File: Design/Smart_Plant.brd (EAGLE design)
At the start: 80 x 111.8 mm, 85 parts, among them IC1 NE555D, Q1 IRLML0100, Q3 2.5A/30V, Q4 MBT3904DW1T1, U10 ESP3212, U6 W25Q32FVSS, U7 FT231XS, U8 MCP73831, U9 AP2112K-3.3V, X2 MICROSD, Y3 26MHz

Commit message: Updated design files for Smart_Plant
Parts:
- removed C29, C30: 10pF, SparkFun-Capacitors:0603
- removed C31, C32: 270pF, esp32-thing-temp:0603
- removed C33: 10nF, SparkFun-Capacitors:0603
- removed C34, C37, C38, C41, C48, C49, C51, C53: 0.1uF, SparkFun-Capacitors:0603
- removed C35: 2.4pF, esp32-thing-temp:0603
- removed C36: 5.6pF, esp32-thing-temp:0603
- removed C39, C40: 47pF, SparkFun-Capacitors:0603
- removed C42: 4.7uF, SparkFun-Capacitors:0603-CAP
- removed C43: 1.0uF, SparkFun-Capacitors:0805
- removed C44: 2.2uF, SparkFun-Capacitors:0603
- removed C45, C46: 4.7uF, SparkFun-Capacitors:0603
- removed C47: 100pF, SparkFun-Capacitors:0603
- removed C50: 10uF, SparkFun-Capacitors:0603
- removed C52: 1.0uF, SparkFun-Capacitors:0603
- removed C56: 3.0nF, esp32-thing-temp:0603
- removed D10, D9: MBR0530, microbuilder:SOD-123
- removed D5: BAT20J, SparkFun-DiscreteSemi:SOD-323
- removed D6: Yellow, SparkFun-LED:LED-0603
- removed D7: Green, SparkFun-LED:LED-0603
- removed E2: ANTENNA, esp32-thing-temp:TRACE_ANTENNA_2.4GHZ_25.7MM_TUNED
- removed EINK1: EINK_24PIN_290IN, microbuilder:EINK_290IN
- removed F2: 500mA, SparkFun-PowerIC:PTC-1206
- removed JP1: (no value), SparkFun-Connectors:USB-B-MICRO-SMD_V03
- removed JP3: LiPo, SparkFun-Connectors:JST-2-PTH
- removed L2: 2.7nH, SparkFun-Passives:0603
- removed Q3: 2.5A/30V, SparkFun-DiscreteSemi:SOT23-3
- removed Q4: MBT3904DW1T1, esp32-thing-temp:SC70-6
- removed R19, R24: 1K, SparkFun-Resistors:0603
- removed R20: 2.0k, SparkFun-Resistors:0603
- removed R21: DNP, SparkFun-Passives:1/6W-RES
- removed R22, R23, R26: 10k, SparkFun-Resistors:0603
- removed R27: DNP, microbuilder:0805_10MGAP
- removed S3: RESET, SparkFun-Electromechanical:TACTILE_SWITCH_SMD_4.6X2.8MM
- removed S4: BTN-0, SparkFun-Electromechanical:TACTILE_SWITCH_SMD_4.6X2.8MM
- removed SJ4: (no value), SparkFun-Passives:PAD-JUMPER-3-2OF3_NC_BY_TRACE_YES_SILK_FULL_BOX
- removed SJ5: JUMPER-PAD-2-NC_BY_TRACE, SparkFun-Passives:PAD-JUMPER-2-NC_BY_TRACE_YES_SILK
- removed U10: ESP3212, esp32-thing-temp:QFN48-0.4MM
- removed U6: W25Q32FVSS, SparkFun-DigitalIC:SOIC-8
- removed U7: FT231XS, SparkFun-DigitalIC:SSOP20_L
- removed U8: MCP73831, SparkFun-PowerIC:SOT23-5
- removed U9: AP2112K-3.3V, SparkFun-PowerIC:SOT23-5
- removed X2: MICROSD, microbuilder:MICROSD
- removed Y3: 26MHz, things:CRYSTAL-SMD-3.2X2.5
- added BT1: (no value), SparkFun-Batteries:BATTCOM_20MM_PTH
- added C10, C16, C4: 10uF, rcl:C0603
- added C11, C6: 100nF, rcl:C0603
- added C12: 22uF, rcl:C0603
- added C15: 0.1uF, rcl:C0603
- added C5: 10nF, rcl:C0603
- added C7: 1uF, rcl:C0603
- added D1, D2, D3: SS14, SparkFun-DiscreteSemi:SMA-DIODE
- added FPC: E-PAPER-FPC, SpaceDIY_connectors:FPC-05FB-24PH20
- added IC2: TLC555CDR, linear:SO08
- added IC3: AHT20, SamacSys_Parts:AHT20
- added IC4: TP4056, TP4056:SOT23-8
- added J1: (no value), SparkFun-Connectors:1X02
- added J3: (no value), pinhead:1X04
- added LED1: Red, SpaceDIY_semiconductors:LED_0603
- added LED2: Green, SpaceDIY_semiconductors:LED_0603
- added Q2: ALS-PT19-315C, SparkFun-DiscreteSemi:PT17-21C-L41-TR8
- added R14, R7: 10k, rcl:R0603
- added R17: 220, rcl:R0603
- added R4: 33k, rcl:R0603
- added R5: 1K, rcl:R0603
- added R6: 1k, rcl:R0603
- added R8: 1M, rcl:R0603
- added R9: 10K, rcl:R0603
- added S1: Flash, SpaceDIY_electromechanical:TACTILE_SWITCH_SMD_5.2MM
- added S2: Reset, SpaceDIY_electromechanical:TACTILE_SWITCH_SMD_5.2MM
- added T1: MMBT2222A, JLC PCB Basic Parts_loc:SOT23
- added T2: LBSS84LT1G, JLC PCB Basic Parts_loc:SOT23
- added TP1, TP2: TPB1,27, testpad:B1,27
- added U1: ESP-32S, esp32:ESP-32S
- C1: value 0.1uF -> 10uF; device SparkFun-Capacitors:0603 -> rcl:C0603
- C13, C14, C17, C18, C19, C25, C27, C28, C9: device microbuilder:0805-NO -> rcl:C0603
- C2: value 0.1uF -> 4.7uF; device SparkFun-Capacitors:0603 -> rcl:C0603
- C26: value 4.7uF/25V -> 4.7uF; device microbuilder:0805-NO -> rcl:C0603
- C3: value 0.1uF -> 0.47nF; device SparkFun-Capacitors:0603 -> rcl:C0603
- C8: value 10uF/10V+ -> 10uF; device microbuilder:0805-NO -> rcl:C0603
- D4: value MBR0530 -> LL4148; device microbuilder:SOD-123 -> SpaceDIY_semiconductors:LL-34
- IC1: value NE555D -> AMS1117-3.3; device linear:SO08 -> SparkFun-IC-Power:SOT223
- R1, R12, R15: value 27 -> 10k; device SparkFun-Resistors:0603 -> rcl:R0603
- R10, R16: device SparkFun-Resistors:0603 -> rcl:R0603
- R11: value 20k -> 1k; device SparkFun-Resistors:0603 -> rcl:R0603
- R13: value 0.47ohm -> 0.47; device microbuilder:0805_10MGAP -> rcl:R0603
- R2: value 27 -> 330R; device SparkFun-Resistors:0603 -> rcl:R0603
- R3: value 27 -> 1.5k; device SparkFun-Resistors:0603 -> rcl:R0603
- moved R1 121.0 mm to (74.0, 6.00)
- moved C1 119.1 mm to (2.50, 29.0), turned to 270 degrees
- moved C2 118.5 mm to (55.5, 3.00), turned to 180 degrees
- moved C3 109.3 mm to (26.5, 4.50), turned to 180 degrees
- moved IC1 103.6 mm to (15.0, 29.0), turned to 180 degrees
- moved R3 101.8 mm to (38.0, 2.50), turned to 90 degrees
- moved R2 92.4 mm to (26.5, 2.00)
- moved C8 47.9 mm to (20.0, 32.0), turned to 270 degrees
- moved R10 39.3 mm to (57.0, 16.5), turned to 180 degrees
- moved R11 33.0 mm to (51.0, 16.5), turned to 0 degrees
- moved D4 14.8 mm to (45.0, 2.50), turned to 270 degrees
- moved R15 13.0 mm to (58.0, 27.7), turned to 90 degrees
- moved R16 9.45 mm to (58.0, 24.5)
- moved R12 4.39 mm to (48.0, 12.5)
- moved R13 2.12 mm to (74.0, 8.51), turned to 0 degrees
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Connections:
- removed net 0: Q4.6, R26.1, S4.3, S4.4, U10.23
- removed net 12: U10.18
- removed net 19: U10.38
- removed net 21: U10.42
- removed net 22: U10.39
- removed net 25: U10.14
- removed net 26: U10.15
- removed net 27: U10.16
- removed net 3.3V_F: C41.1, U7.13, U7.14, U7.3
- removed net 32: U10.12
- removed net 33: U10.13
- removed net 34: U10.10
- removed net 35: U10.11
- removed net 36: C31.2, U10.5
- removed net 37: C31.1, U10.6
- removed net 38: C32.1, U10.7
- removed net 39: C32.2, U10.8
- removed net 3V3: C44.1, C47.1, C48.1, C49.1, C50.1, C51.1, C53.1, C8.2, EINK1.15, EINK1.16, L3.P$2, R10.2, R24.1, R26.2, SJ4.3, U10.1, U10.19, U10.3, U10.37, U10.4, U10.43, U10.46, U9.5, X2.4
- removed net CAP_10N1: C33.2, C56.1, R11.2, U10.48
- removed net CHIP_PU: Q4.3, R10.1, S3.3, S3.4, U10.9
- removed net D+: C39.1, JP1.D+, R15.1
- removed net D-: C40.1, JP1.D-, R12.1
- removed net DTR: Q4.1, R22.1, U7.1
- removed net FLASH_SCK: U10.31, U6.6
- removed net FLASH_SCS: U10.30, U6.1
- removed net FLASH_SDI: U10.33, U6.5
- removed net FLASH_SDO: U10.32, U6.2
- removed net FLASH_SHD: U10.28, U6.7
- removed net FLASH_SWP: U10.29, U6.3
- removed net FLASH_VDD: C52.1, SJ4.1, U10.26
- removed net LNA_IN1: C36.1, L2.1, U10.2
- removed net MISO_SD: U10.22, X2.7
- removed net MOSI_SD: U10.21, X2.3
- removed net N$19: D6.A, R19.2
- removed net N$20: D6.C, U8.1
- removed net N$21: R21.2, SJ5.2, U8.5
- removed net N$22: R20.2, SJ5.1
- removed net N$23: Q4.5, R22.2
- removed net N$24: Q4.2, R23.2
- removed net N$25: C29.2, U10.45, Y3.1
- removed net N$26: C30.2, U10.44, Y3.3
- removed net N$27: D7.A, R24.2
- removed net N$30: C56.2, R11.1, U10.47
- removed net RTS: Q4.4, R23.1, U7.2
- removed net SCLK_SD: U10.17, X2.5
- removed net SDCS_SD: U10.20, X2.2
- removed net SHIELD: JP1.SHIELD1, JP1.SHIELD2, JP1.SHIELD3
- removed net TRACE_ANT1: C35.1, C36.2, E2.ANT
- removed net TSCL: EINK1.6
- removed net TSDA: EINK1.7
- removed net U0RXD: U10.40, U7.20
- removed net U0TXD: U10.41, U7.4
- removed net V+: IC1.8
- removed net VUSB-RAW: C37.1, F2.1, JP1.VBUS
- removed net V_BATT: C45.1, JP3.2, Q3.3, U8.3
- removed net V_USB: C38.1, C42.1, C46.1, D5.A, F2.2, Q3.1, R16.2, R19.1, U7.15, U8.4
- new net 3.3V: C10.1, C11.1, C12.1, C2.1, FPC.15, FPC.16, IC1.2, J3.1, L3.P$2, R10.1, R12.1, R9.2, T2.2, U1.2
- new net IO0: R12.2, S1.3, U1.25
- new net LIGHT: Q2.E, R14.1, U1.9
- new net MOISTURE: C7.1, D4.C, R8.1, U1.8
- new net N$1: IC4.2, R4.2
- new net N$10: C15.1, C16.1, IC3.2, R17.2
- new net N$2: IC4.6, R6.2
- new net N$3: LED1.C, R5.1
- new net N$4: LED2.C, R6.1
- new net N$7: IC2.7, R2.2, R3.1
- new net N$8: C5.2, IC2.5
- new net N$9: R10.2, T1.3, T2.1
- new net OUT: IC2.3, R7.2, TP1.TP
- new net PROBE: D4.A, R7.1
- new net RST: R9.1, S2.3, U1.3
- new net RX: J3.4, U1.34
- new net SCL: IC3.3, R15.2, U1.36
- new net SDA: IC3.4, R16.2, U1.33
- new net SENS: R11.1, U1.27
- new net TX: J3.3, U1.35
- new net VBAT: BT1.1, C4.1, C8.1, IC1.3, IC4.5
- new net VSENS: C6.1, IC2.4, IC2.8, Q2.C, R15.1, R16.1, R17.1, R2.1, T2.3, TP2.TP
- net BUSY: now also FPC.9, U1.10; no longer EINK1.9, U10.24
- net DC: now also FPC.11, U1.12; no longer EINK1.11, U10.27
- net DISPCS: now also FPC.12, U1.23; no longer EINK1.12, U10.34
- net GDR: now also FPC.2, R1.1; no longer EINK1.2
- net GND: now also BT1.2, C1.2, C10.2, C11.2, C12.2, C15.2, C16.2, C2.2, C3.2, C4.2, C5.1, C6.2, C7.2, C8.2, D2.C, FPC.17, FPC.8, IC2.1, IC3.5, IC4.3, IC4.8, J1.2, J3.2, R1.2, R14.2, R4.1, R8.2, S1.1, S2.1, T1.2, U1.1, U1.15, U1.38, U1.GND; no longer C29.1, C30.1, C33.1, C34.2, C35.2, C37.2, C38.2, C39.2, C40.2, C41.2, C42.2, C43.2, C44.2, C45.2, C46.2, C47.2, C48.2, C49.2, C50.2, C51.2, C52.2, C53.2, C8.1, D4.C, D7.C, E2.GND, E2.GND2, EINK1.17, EINK1.8, JP1.GND, JP3.1, L2.2, R16.1, R20.1, R21.1, R27.2, S3.1, S3.2, S4.1, S4.2, U10.EP, U6.4, U7.16, U7.6, U8.2, U9.2, X2.6, X2.MT1, X2.MT2, Y3.2, Y3.4
- net MOSI: now also FPC.14, U1.13; no longer EINK1.14, U10.36
- net N$11: now also FPC.5; no longer EINK1.5
- net N$12: now also FPC.18; no longer EINK1.18
- net N$13: now also FPC.20; no longer EINK1.20
- net N$14: now also FPC.22; no longer EINK1.22
- net N$15: now also FPC.24; no longer EINK1.24
- net N$16: now also D2.A, D3.C; no longer D4.A, D9.C
- net N$17: now also D1.A; no longer D10.A
- net N$18: now also R11.2, T1.1; no longer R15.2, U7.11
- net N$31: now also FPC.4; no longer EINK1.4
- net N$32: now also FPC.19; no longer EINK1.19
- net N$5: now also C3.1, IC2.2, IC2.6, R3.2; no longer C34.1, SJ4.2, U6.8
- net N$6: now also IC4.7, R5.2; no longer R12.2, U7.12
- net RESE: now also FPC.3; no longer EINK1.3, R27.1
- net RESET: now also FPC.10, U1.11; no longer EINK1.10, U10.25
- net SCLK: now also FPC.13, U1.16; no longer EINK1.13, U10.35
- net VGH: now also D1.C, FPC.21; no longer D10.C, EINK1.21
- net VGL: now also D3.A, FPC.23; no longer D9.A, EINK1.23
- net VIN: now also C1.1, IC4.1, IC4.4, J1.1, LED1.A, LED2.A; no longer C43.1, D5.C, Q3.2, U9.1, U9.3
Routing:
- net 3.3V: track 0.00 -> 146.4 mm, vias 0 -> 3
- net VSENS: track 0.00 -> 102.9 mm, vias 0 -> 5
- net PROBE: track 0.00 -> 77.6 mm
- net 3V3: track 74.1 -> 0.00 mm, vias 8 -> 0
- net 0: track 62.2 -> 0.00 mm, vias 3 -> 0
- net RST: track 0.00 -> 59.1 mm, vias 0 -> 2
- net CHIP_PU: track 56.5 -> 0.00 mm, vias 4 -> 0
- net IO0: track 0.00 -> 49.2 mm, vias 0 -> 2
- net U0RXD: track 45.4 -> 0.00 mm, vias 4 -> 0
- net V_USB: track 43.1 -> 0.00 mm, vias 2 -> 0
- net U0TXD: track 41.0 -> 0.00 mm, vias 4 -> 0
- net RX: track 0.00 -> 37.9 mm, vias 0 -> 2
- net MOISTURE: track 0.00 -> 36.0 mm, vias 0 -> 2
- net TX: track 0.00 -> 33.7 mm, vias 0 -> 2
- net SCLK: track 10.2 -> 42.6 mm, vias 1 -> 2
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- removed copper zone on layer 1, net SHIELD
- removed copper zone on layer 16, net SHIELD
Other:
- board size 80 x 111.8 mm -> 80 x 129.1 mm
- board text added: "CHRG"
- board text added: "JLCJLCJLCJLC"
- board text added: "SIG"
- board text added: "STDBY"
- board text added: "Vsens"
- board text removed: "!RST!"
- board text removed: "0"
- board text removed: "12"
- board text removed: "13"
- board text removed: "14"
- board text removed: "15"
- board text removed: "16"
- board text removed: "17"
- board text removed: "18"
- board text removed: "19"
- board text removed: "2"
- board text removed: "21"
- board text removed: "22"
- board text removed: "23"
- board text removed: "25"
- board text removed: "26"
- board text removed: "27"
- board text removed: "32"
- board text removed: "33"
- board text removed: "34"
- board text removed: "35"
- board text removed: "36"
- board text removed: "37"
- board text removed: "38"
- board text removed: "39"
- board text removed: "3V3"
- board text removed: "4"
- board text removed: "5"
- board text removed: "Adafruit Industries"
- board text removed: "CHG PROG"
- board text removed: "E-Ink Display"
- board text removed: "FLASH VCC"
- board text removed: "GND"
- board text removed: "IC"
- board text removed: "RST"
- board text removed: "RX"
- board text removed: "RXI"
- board text removed: "TX"
- board text removed: "TXO"
- board text removed: "VBAT"
- board text removed: "VUSB"

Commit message: Update design files
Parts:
- removed BT1: (no value), SparkFun-Batteries:BATTCOM_20MM_PTH
- removed J3: (no value), pinhead:1X04
- added J2: USBC-6P, SpaceDIY_connectors:USCX-06FX-XXMX-01
- added J4: (no value), SparkFun-Connectors:JST-2-PTH-NS
- added J5: (no value), SparkFun-Connectors:1X04
- added R18: 240k, rcl:R0603
- added R19: 1M, rcl:R0603
- R4: value 33k -> 1.2k
- moved R9 3.08 mm to (20.0, 24.3)
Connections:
- new net BATTERY: R18.1, R19.2, U1.7
- net 3.3V: now also J5.1; no longer J3.1
- net GND: now also J2.GND1, J2.GND2, J4.1, J5.2, R18.2; no longer BT1.2, J3.2
- net RX: now also J5.4; no longer J3.4
- net TX: now also J5.3; no longer J3.3
- net VBAT: now also J4.2, R19.1; no longer BT1.1
- net VIN: now also J2.VBUS1, J2.VBUS2
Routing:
- net BATTERY: track 0.00 -> 25.8 mm
- net VBAT: track 25.0 -> 50.4 mm, vias 0 -> 1
- net VIN: track 26.7 -> 46.9 mm, vias 0 -> 2
- net 3.3V: track 146.4 -> 142.9 mm, vias 3 -> 6
- net RST: track 59.1 -> 62.4 mm
- net TX: track 33.7 -> 34.2 mm
- net GND: vias 23 -> 24

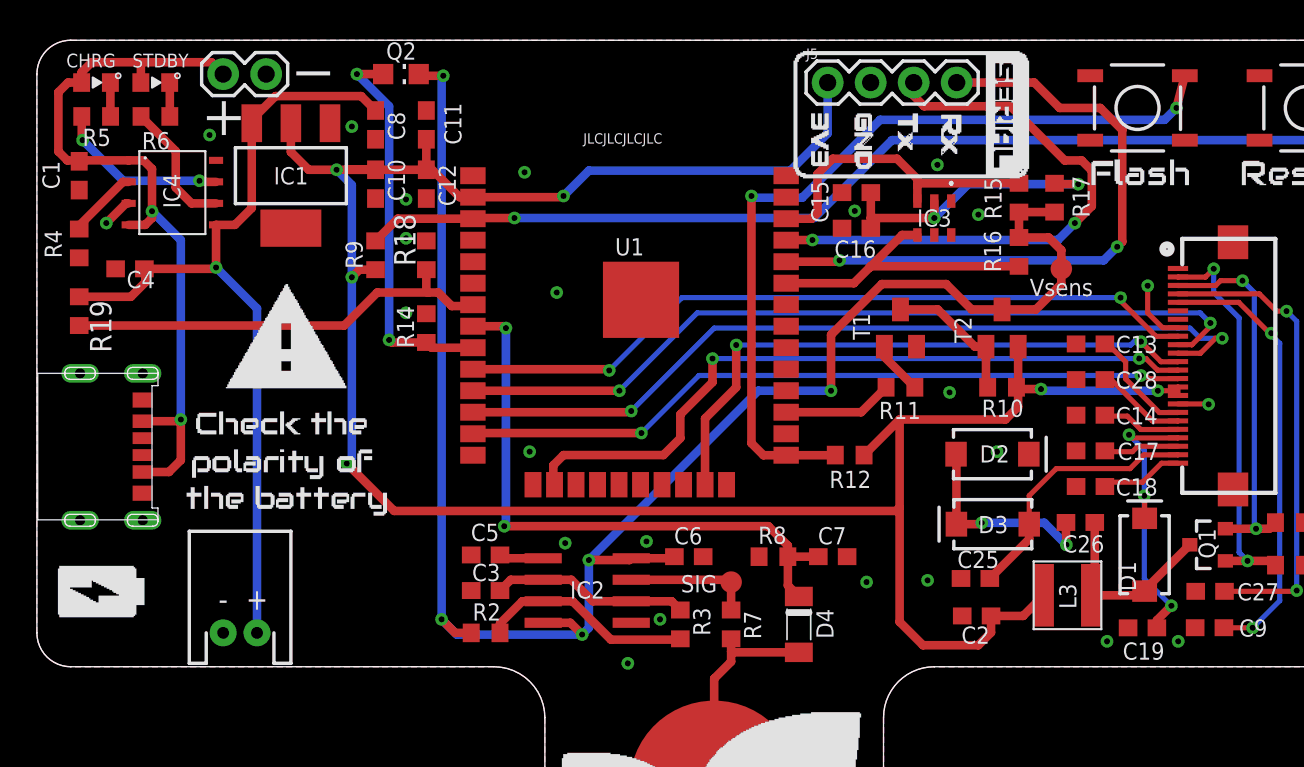
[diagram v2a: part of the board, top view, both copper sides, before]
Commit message: Added designs for V1R2
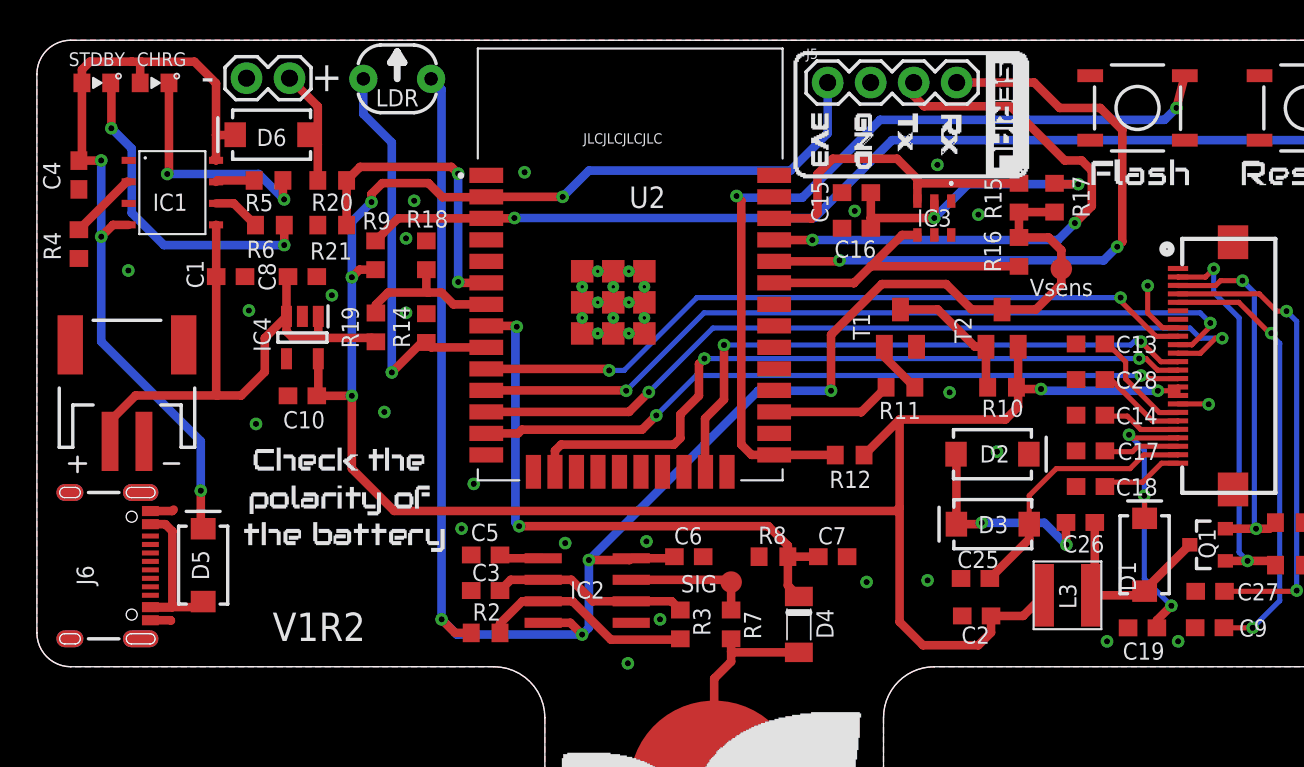
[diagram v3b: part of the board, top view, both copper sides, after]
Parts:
- removed C11: 100nF, rcl:C0603
- removed C12: 22uF, rcl:C0603
- removed J2: USBC-6P, SpaceDIY_connectors:USCX-06FX-XXMX-01
- removed Q2: ALS-PT19-315C, SparkFun-DiscreteSemi:PT17-21C-L41-TR8
- removed U1: ESP-32S, esp32:ESP-32S
- added D5, D6: SS14, SpaceDIY_semiconductors:SMA-DIODE
- added J6: USB-C, SparkFun-Connectors:USB-C-16P-4LAYER-ISOLATED
- added LDR: PHOTOCELLPTH, SparkFun-Sensors:PHOTOCELL
- added R20: 1M, rcl:R0603
- added R21: 240k, rcl:R0603
- added U2: ESP32-WROOM-32, ESP32-WROOM-32:MODULE_ESP32-WROOM-32
- D1, D2, D3: device SparkFun-DiscreteSemi:SMA-DIODE -> SpaceDIY_semiconductors:SMA-DIODE
- IC1: value AMS1117-3.3 -> TP4056; device SparkFun-IC-Power:SOT223 -> TP4056:SOT23-8
- IC4: value TP4056 -> RT9080-33GJ5; device TP4056:SOT23-8 -> SamacSys_Parts:SOT94P280X100-5N
- J4: device SparkFun-Connectors:JST-2-PTH-NS -> SpaceDIY_connectors:JST-2-SMD
- R18: value 240k -> 1M
- moved R19 17.5 mm to (20.0, 20.0), turned to 90 degrees
- moved J4 16.7 mm to (5.32, 17.3), turned to 180 degrees
- moved C10 13.2 mm to (15.7, 16.0), turned to 180 degrees
- moved IC4 11.5 mm to (15.7, 19.4)
- moved R5 10.9 mm to (13.7, 28.7)
- moved C1 10.7 mm to (11.4, 23.0), turned to 0 degrees
- moved C8 9.95 mm to (15.7, 23.0), turned to 0 degrees
- moved R6 9.32 mm to (13.8, 26.1)
- moved IC1 7.07 mm to (8.00, 28.0), turned to 270 degrees
- moved C4 6.31 mm to (2.48, 29.0), turned to 270 degrees
- moved J1 3.93 mm to (14.9, 34.8), turned to 180 degrees
- moved LED2 3.48 mm to (3.52, 34.5)
- moved LED1 3.46 mm to (6.96, 34.5)
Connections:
- removed net N$2 (its old number): IC4.6, R6.2
- new net D+: J6.A6, J6.B6
- new net D-: J6.A7, J6.B7
- new net N$4: IC1.2, R4.2
- new net N$46: D6.A, J1.1, R20.1
- new net VSOLAR: R20.2, R21.2, U2.6
- new net V_USB: D5.A, J6.VBUS1, J6.VBUS2
- net 3.3V: now also IC4.5, U2.2; no longer C11.1, C12.1, IC1.2, U1.2
- net BATTERY: now also U2.7; no longer U1.7
- net BUSY: now also U2.10; no longer U1.10
- net DC: now also U2.12; no longer U1.12
- net DISPCS: now also U2.23; no longer U1.23
- net GND: now also IC1.3, IC4.2, J4.2, J6.GND, J6.GND2, R21.1, U2.1, U2.15, U2.38, U2.39_1, U2.39_10, U2.39_11, U2.39_12, U2.39_13, U2.39_14, U2.39_15, U2.39_16, U2.39_17, U2.39_18, U2.39_19, U2.39_2, U2.39_20, U2.39_21, U2.39_3, U2.39_4, U2.39_5, U2.39_6, U2.39_7, U2.39_8, U2.39_9; no longer C11.2, C12.2, IC4.3, IC4.8, J2.GND1, J2.GND2, J4.1, U1.1, U1.15, U1.38, U1.GND
- net IO0: now also U2.25; no longer U1.25
- net LIGHT: now also LDR.1, U2.9; no longer Q2.E, U1.9
- net MOISTURE: now also U2.8; no longer U1.8
- net MOSI: now also U2.13; no longer U1.13
- net N$1: now also IC1.6, R6.2; no longer IC4.2, R4.2
- net N$6: now also IC1.7; no longer IC4.7
- net RESET: now also U2.11; no longer U1.11
- net RST: now also U2.3; no longer U1.3
- net RX: now also U2.34; no longer U1.34
- net SCL: now also U2.36; no longer U1.36
- net SCLK: now also U2.16; no longer U1.16
- net SDA: now also U2.33; no longer U1.33
- net SENS: now also U2.27; no longer U1.27
- net TX: now also U2.35; no longer U1.35
- net VBAT: now also C1.1, IC1.5, IC4.1, IC4.3, J4.1; no longer C4.1, IC1.3, IC4.5, J4.2
- net VIN: now also C4.1, D5.C, D6.C, IC1.4, IC1.8; no longer C1.1, IC4.1, IC4.4, J1.1, J2.VBUS1, J2.VBUS2
- net VSENS: now also LDR.2; no longer Q2.C
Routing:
- net VSOLAR: track 0.00 -> 17.8 mm, vias 0 -> 2
- net N$3: track 2.00 -> 19.2 mm, vias 0 -> 2
- net BATTERY: track 25.8 -> 8.99 mm
- net VBAT: track 50.4 -> 35.7 mm, vias 1 -> 0
- net N$2: track 2.00 -> 14.1 mm, vias 0 -> 2
- net V_USB: track 0.00 -> 10.5 mm
- net N$6: track 10.3 -> 2.29 mm, vias 2 -> 0
- net 3.3V: track 142.9 -> 135.0 mm
- net N$2 (its old number): track 7.82 -> 0.00 mm
- net N$46: track 0.00 -> 7.55 mm
- net N$4: track 0.00 -> 4.11 mm
- net VIN: track 46.9 -> 48.7 mm, vias 2 -> 3
- net IO0: track 49.2 -> 50.9 mm
- net VSENS: track 102.9 -> 101.5 mm, vias 5 -> 4
- net N$1: track 4.19 -> 2.86 mm
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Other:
- board text added: "+"
- board text added: "-"
- board text added: "V1R2"

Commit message: SoC first draft
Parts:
- removed LDR: PHOTOCELLPTH, SparkFun-Sensors:PHOTOCELL
- removed R12: 10k, rcl:R0603
- removed R19: 1M, rcl:R0603
- removed R9: 10K, rcl:R0603
- added C11: 100nF, rcl:C0603
- added C20: 2.4pF, esp32-thing-temp:0603
- added C21: 5.6pF, esp32-thing-temp:0603
- added C40: 1uF, rcl:C0603
- added C46, C48, C55, C57, C62, C63: 1uF, microbuilder:_0402NO
- added C47, C52, C53, C54, C56, C58: 0.1uF, microbuilder:_0402NO
- added C49: 22uF, microbuilder:0805-NO
- added C59, C60: 16pF, microbuilder:_0402NO
- added C61: 1uF, SpaceDIY_passive_components:C0402
- added E2: ANTENNA, esp32-thing-temp:TRACE_ANTENNA_2.4GHZ_25.7MM_TUNED
- added IC5: LC709203F/MH, adafruit_sensor:WLCSP9
- added IC6: VEML7700-TR, SpaceDIY_sensors:VEML7700
- added L2: 2.7nH, SparkFun-Passives:0603
- added L5: 2nH, microbuilder:_0402NO
- added R29: 0, microbuilder:_0402NO
- added R30: 1Meg, microbuilder:_0402NO
- added R31: 10K, SpaceDIY_passive_components:R0402
- added U$42: (no value), itsy_silks:QTPY_ESP32_TOP
- added X5: ESP32-S3QFN54, adafruit_wireless:QFN56_7X7
- added Y2: 40MHz, microbuilder:CRYSTAL_2X1.6
- R14: value 10k -> 1M
- moved R18 154.0 mm to (-68.3, -99.7), turned to 0 degrees
- moved R14 146.7 mm to (-68.3, -94.8), turned to 0 degrees
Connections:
- new net !RESET: C61.1, R31.2, S2.3, X5.4
- new net A2: X5.14
- new net A3: X5.13
- new net IO10_DBLTAP: C62.1, R30.2, X5.15
- new net LNA_IN1: C21.1, L2.1, X5.1
- new net MISO: X5.42
- new net N$53: C59.1, X5.54, Y2.3
- new net N$54: C60.1, R29.1, Y2.1
- new net N$55: R29.2, X5.53
- new net NEOPIX: X5.44
- new net NEOPIX_PWR: X5.43
- new net SCK: X5.41
- new net SCL1: X5.45
- new net SDA1: X5.47
- new net TRACE_ANT1: C20.1, C21.2, E2.ANT
- new net VDD3P3: C47.1, L5.2, X5.2, X5.3
- new net VDD_SPI: C54.1, C55.1, X5.29
- net 3.3V: now also C46.1, C48.1, C49.1, C52.1, C53.1, C56.1, C57.1, C58.1, C63.1, L5.1, R31.1, X5.20, X5.27, X5.46, X5.55, X5.56; no longer R12.1, R9.2
- net BATTERY: now also R14.2, X5.24; no longer R19.2
- net D+: now also X5.26
- net D-: now also X5.25
- net GND: now also C11.2, C20.2, C40.2, C46.2, C47.2, C48.2, C49.2, C52.2, C53.2, C54.2, C55.2, C56.2, C57.2, C58.2, C59.2, C60.2, C61.2, C62.2, C63.2, E2.GND, E2.GND2, IC5.A1, IC5.B1, IC6.3, L2.2, R30.1, X5.57; no longer R14.2
- net IO0: now also X5.5; no longer R12.2
- net LIGHT: no longer LDR.1, R14.1
- net MOISTURE: now also X5.23
- net MOSI: now also X5.40
- net RST: no longer R9.1, S2.3
- net RX: now also X5.50
- net SCL: now also IC5.C2, IC6.1, X5.11
- net SDA: now also IC5.C1, IC6.4, X5.12
- net SENS: now also X5.9
- net TX: now also X5.49
- net VBAT: now also C40.1, IC5.A3, R14.1; no longer R19.1
- net VSENS: now also C11.1, IC6.2; no longer LDR.2
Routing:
- net VSENS: track 101.5 -> 69.3 mm
- net LIGHT: track 24.5 -> 3.25 mm, vias 1 -> 0
- net LNA_IN1: track 0.00 -> 8.01 mm
- net GND: track 8.21 -> 12.3 mm, vias 26 -> 73
- net 3.3V: track 135.0 -> 131.1 mm
- net TRACE_ANT1: track 0.00 -> 3.59 mm
- net RST: track 62.4 -> 59.5 mm
- net IO0: track 50.9 -> 48.9 mm
- net BATTERY: track 8.99 -> 7.25 mm
- added copper zone on layer 15, net 3.3V
- added copper zone on layer 2, net GND
